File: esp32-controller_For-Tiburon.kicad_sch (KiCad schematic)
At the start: 15 parts, among them J1 PWR_IN, J2 UART1, J3 UART2, J4 I2C_OLED, J5 I2C_PressureSensor, J6 SD_Card_Receptacle, J7 SP1_2_connector, U1 ESP32-S3-WROOM-1

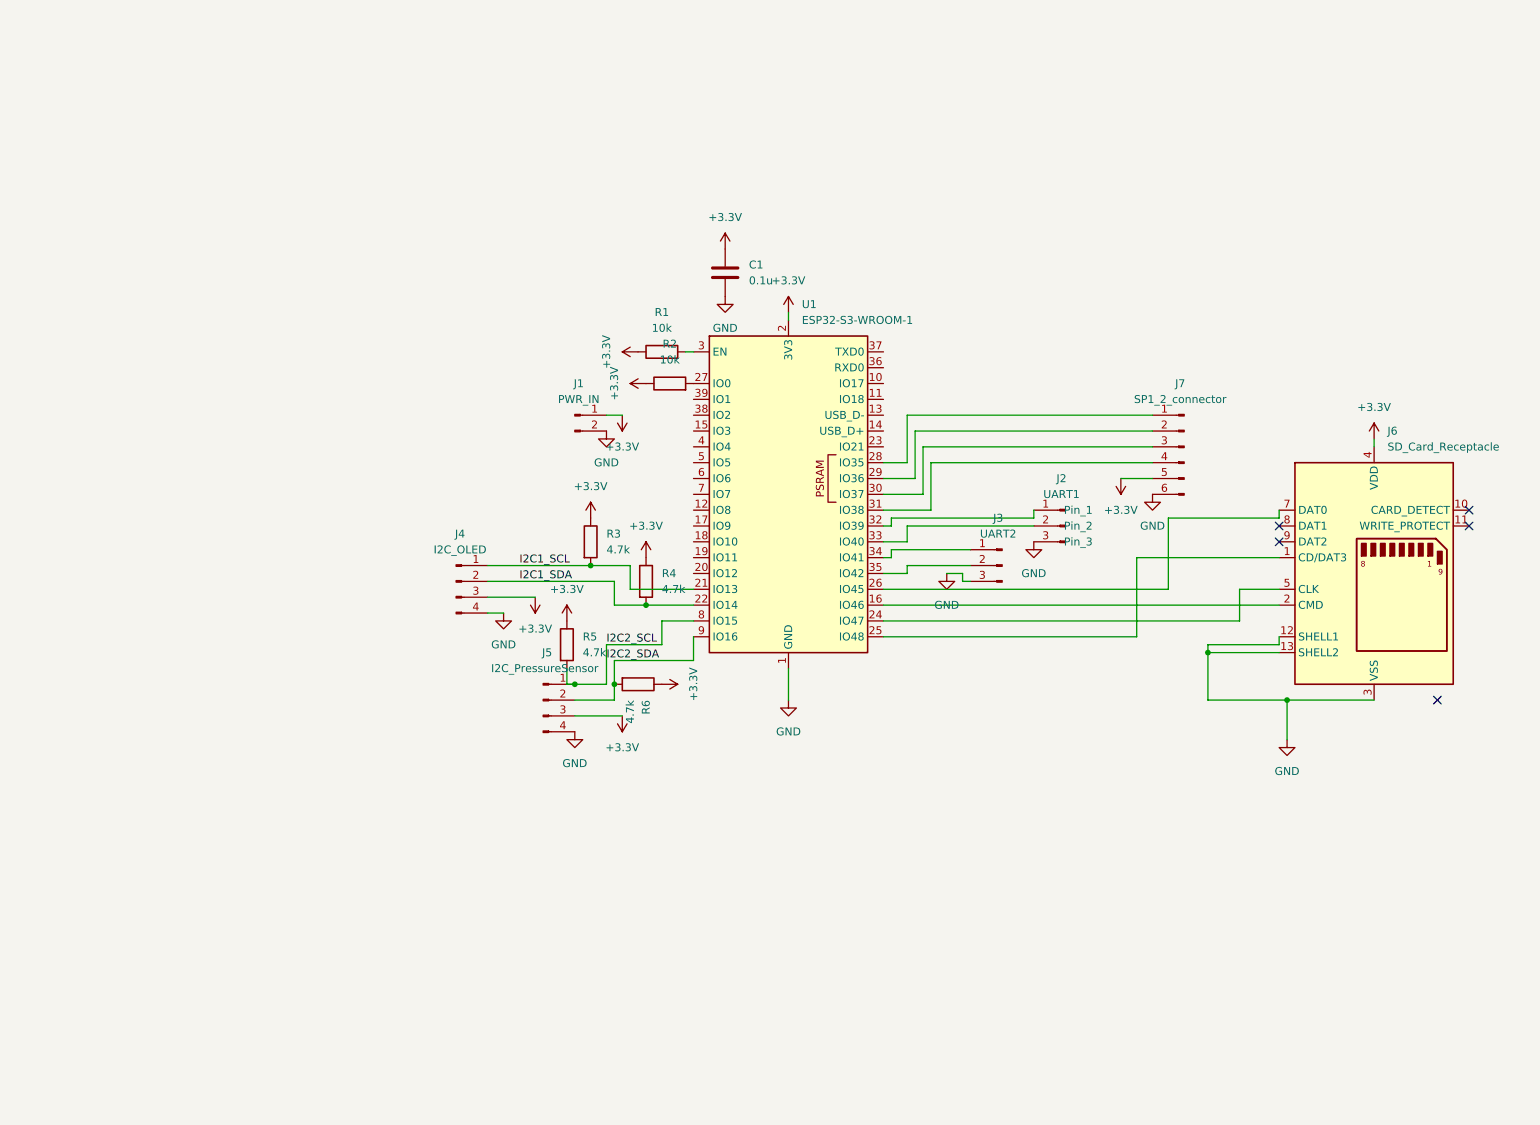
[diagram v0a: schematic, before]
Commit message: Added more of the resistors and added labeling
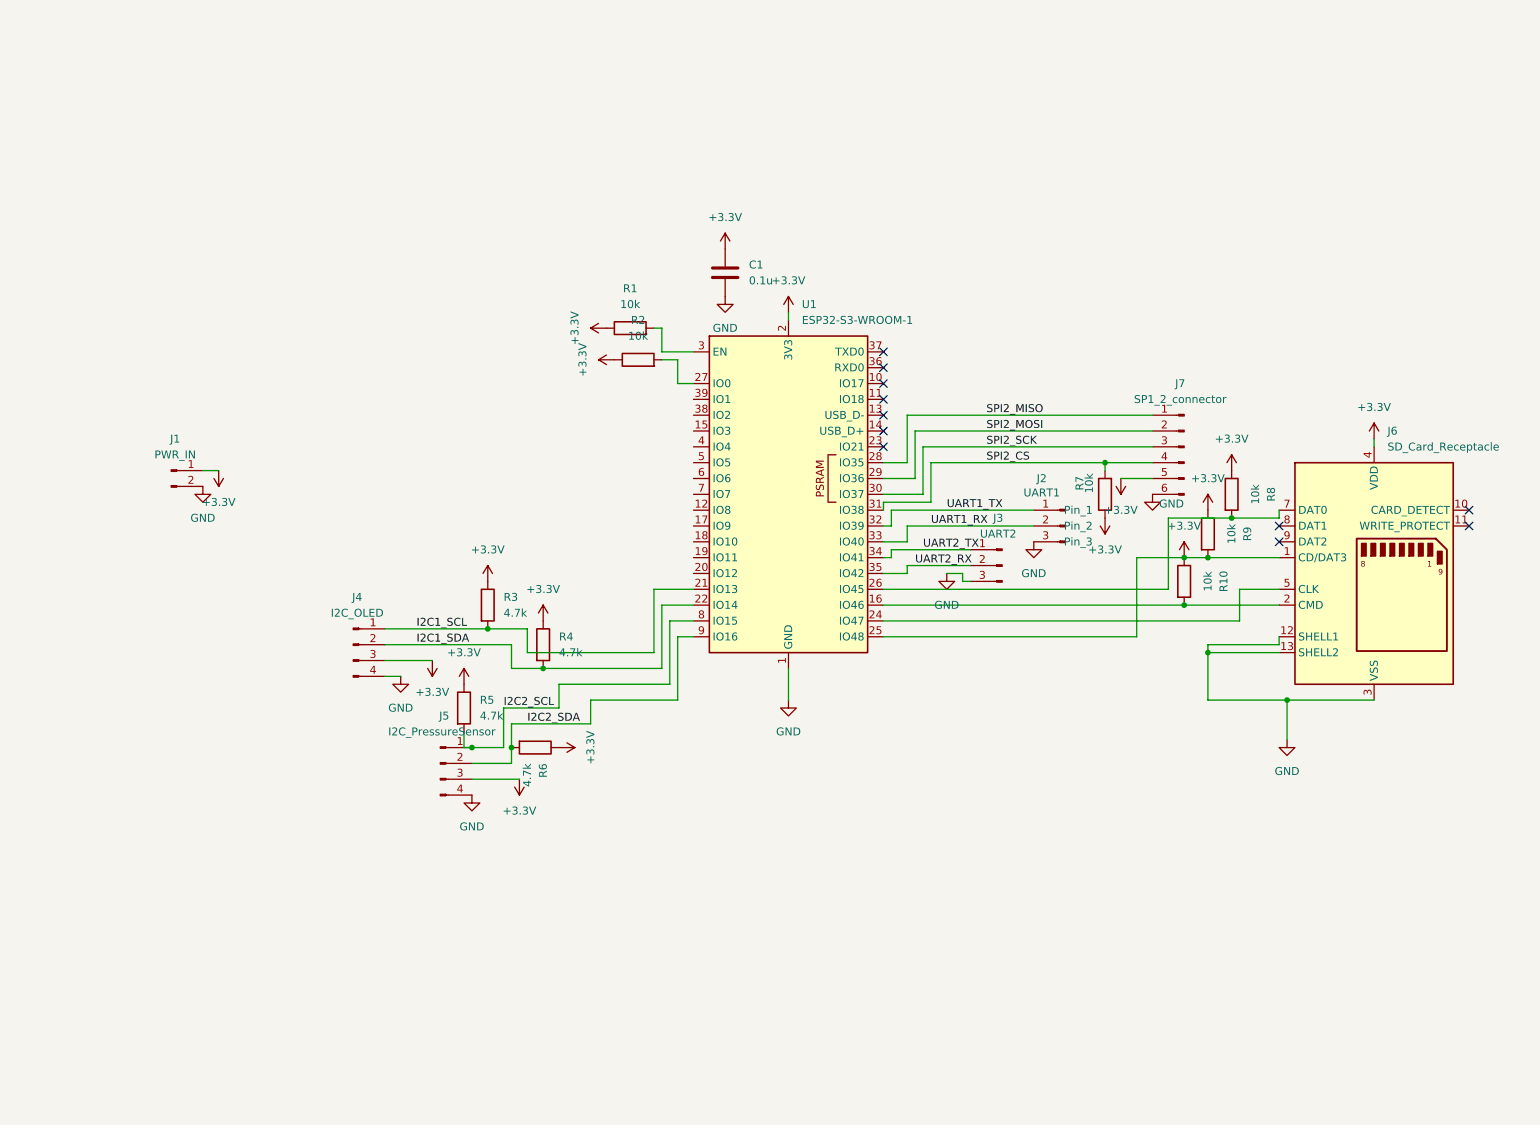
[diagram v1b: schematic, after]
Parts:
- added R10, R7, R8, R9: 10k, symbol Device:R
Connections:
- net +3.3V: now also J6.1 (CD/DAT3), U1.25 (IO48), R10.1, R7.1, R8.1, R9.1, R9.2
- net UART2_TX: now reaches J3.1 (Pin_1), U1.34 (IO41)
- net UART2_RX: now reaches J3.2 (Pin_2), U1.35 (IO42)
- net UART1_TX: now reaches J2.1 (Pin_1), U1.32 (IO39)
- net UART1_RX: now reaches J2.2 (Pin_2), U1.33 (IO40)
- net SPI2_MISO: now reaches J7.1 (Pin_1), U1.28 (IO35)
- net SPI2_MOSI: now reaches J7.2 (Pin_2), U1.29 (IO36)
- net SPI2_SCK: now reaches J7.3 (Pin_3), U1.30 (IO37)
- net SPI2_CS: now reaches J7.4 (Pin_4), U1.31 (IO38)
- net SPI2_CS: now also R7.2
- net I2C2_SDA: now reaches J5.2 (Pin_2), R6.2, U1.9 (IO16)
- net at J6.2 (CMD), U1.16 (IO46): now also R10.2
- net at J6.7 (DAT0), U1.26 (IO45): now also R8.2
- no-connect marks 5 -> 11
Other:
- moved on the sheet: J1, J4, J5, R1, R2, R3, R4, R5, R6

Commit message: Added one thruster and fixed all the resistors into the circuit
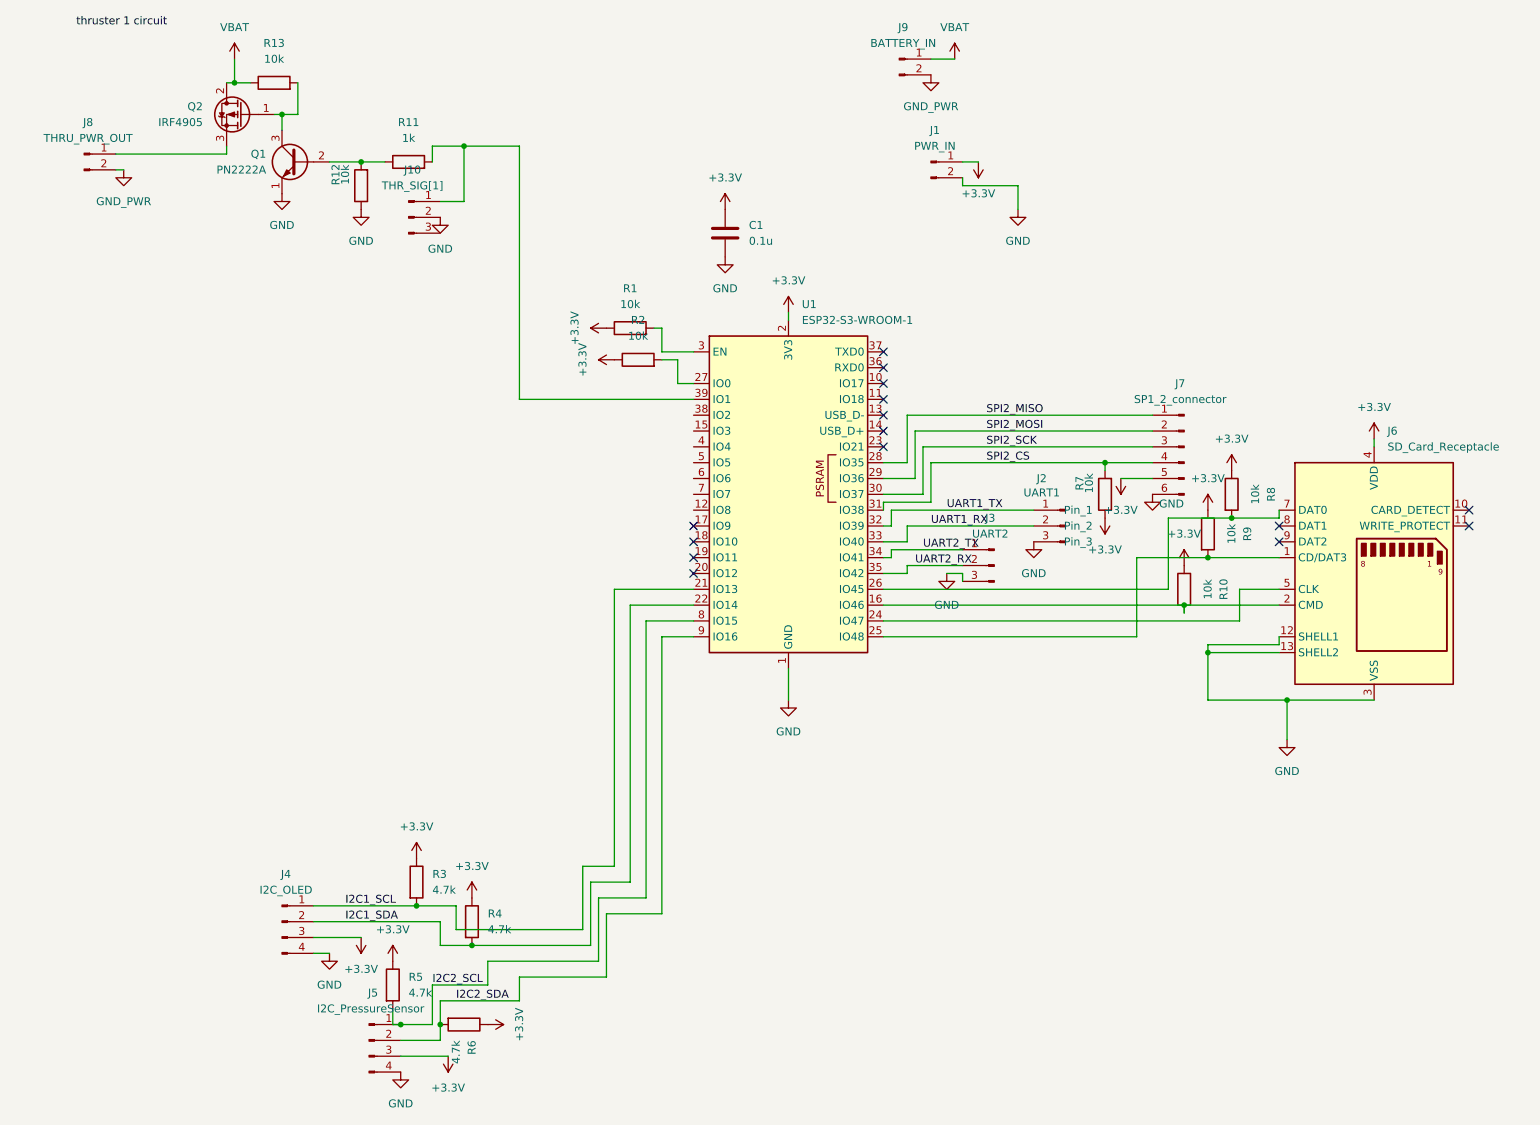
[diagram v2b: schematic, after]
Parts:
- added J10: THR_SIG[1], symbol Connector:Conn_01x03_Pin
- added J8: THRU_PWR_OUT, symbol Connector:Conn_01x02_Pin
- added J9: BATTERY_IN, symbol Connector:Conn_01x02_Pin
- added Q1: PN2222A, Package_TO_SOT_THT:TO-92_Inline, symbol Transistor_BJT:PN2222A
- added Q2: IRF4905, Package_TO_SOT_THT:TO-220-3_Vertical, symbol Transistor_FET:IRF4905
- added R11: 1k, symbol Device:R
- added R12, R13: 10k, symbol Device:R
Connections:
- net +3.3V: no longer J6.1 (CD/DAT3), R9.2, U1.25 (IO48)
- net GND: now also J10.2 (Pin_2), Q1.1 (E), R12.1
- net at U1.39 (IO1): now also J10.1 (Pin_1), R11.2
- new net: J6.1 (CD/DAT3), R9.2, U1.25 (IO48)
- new net: J8.1 (Pin_1), Q2.3 (S)
- new net: Q1.2 (B), R11.1, R12.2
- new net: Q1.3 (C), Q2.1 (G), R13.2
- new net GND_PWR: J8.2 (Pin_2), J9.2 (Pin_2)
- new net VBAT: J9.1 (Pin_1), Q2.2 (D), R13.1
- no-connect marks 11 -> 15
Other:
- moved on the sheet: C1, J1, J3, J4, J5, R10, R3, R4, R5, R6

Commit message: Added thrusters
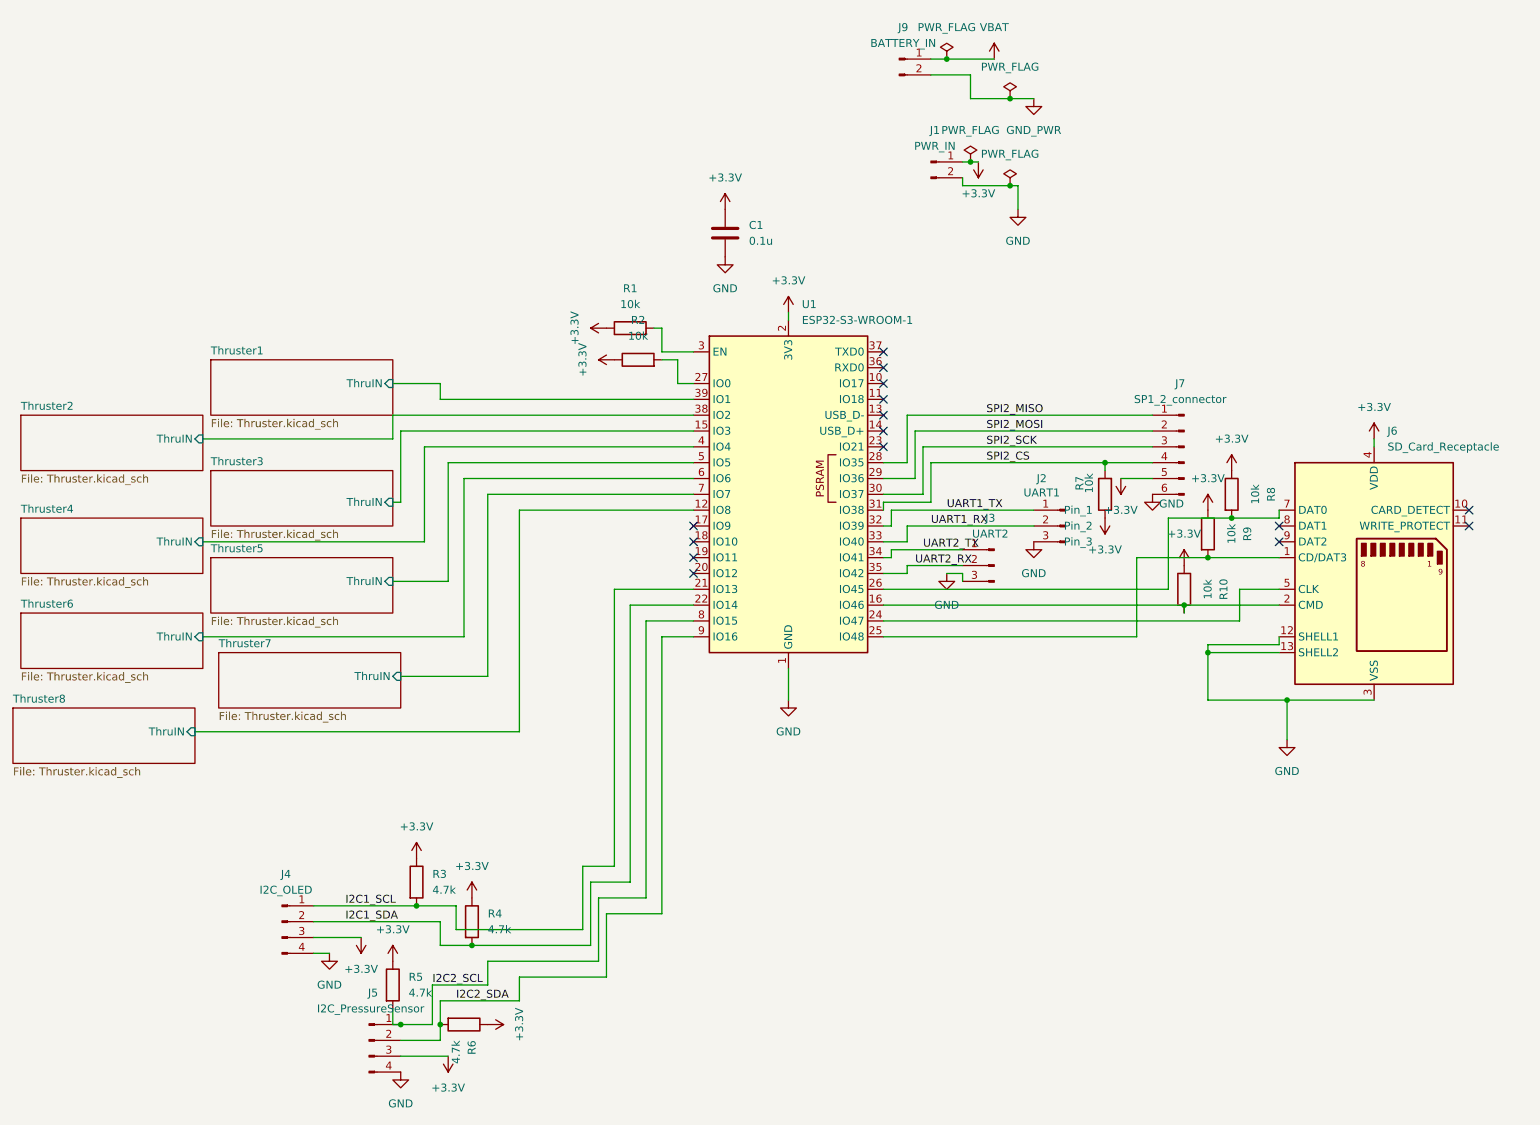
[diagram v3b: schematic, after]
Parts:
- removed J10: THR_SIG[1], symbol Connector:Conn_01x03_Pin
- removed J8: THRU_PWR_OUT, symbol Connector:Conn_01x02_Pin
- removed Q1: PN2222A, Package_TO_SOT_THT:TO-92_Inline, symbol Transistor_BJT:PN2222A
- removed Q2: IRF4905, Package_TO_SOT_THT:TO-220-3_Vertical, symbol Transistor_FET:IRF4905
- removed R11: 1k, symbol Device:R
- removed R12, R13: 10k, symbol Device:R
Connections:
- net Thruster1/ThruIN: now reaches U1.39 (IO1)
- net Thruster8/ThruIN: now reaches U1.12 (IO8)
- net Thruster3/ThruIN: now reaches U1.15 (IO3)
- net Thruster2/ThruIN: now reaches U1.38 (IO2)
- net Thruster4/ThruIN: now reaches U1.4 (IO4)
- net Thruster5/ThruIN: now reaches U1.5 (IO5)
- net Thruster6/ThruIN: now reaches U1.6 (IO6)
- net Thruster7/ThruIN: now reaches U1.7 (IO7)
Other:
- added sheet Thruster1 (Thruster.kicad_sch)
- added sheet Thruster2 (Thruster.kicad_sch)
- added sheet Thruster3 (Thruster.kicad_sch)
- added sheet Thruster4 (Thruster.kicad_sch)
- added sheet Thruster5 (Thruster.kicad_sch)
- added sheet Thruster6 (Thruster.kicad_sch)
- added sheet Thruster7 (Thruster.kicad_sch)
- added sheet Thruster8 (Thruster.kicad_sch)
